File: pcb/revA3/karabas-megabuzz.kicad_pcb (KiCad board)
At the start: 4 copper layers, 92.2 x 44 mm, 173 parts, among them J1 FPGA JTAG, J2 Conn_02x31_Row_Letter_First, J3 uSD card, J4 PJ307, J5 Conn_01x04, J6 PRG, J7 NMI, T1 TestPoint1, T2 TestPoint2, T3 TestPoint, T4 TestPoint, T5 TestPoint, T6 TestPoint, T7 TestPoint, U1 XC6SLX25-FTG256, U10 YMF262-M, U11 SAM2695, U12 PCM5102A, U13 PCM1808PWR, U14 CY62167EV30LL, U15 1117-3.3, U16 1117-3.3, U17 1117-1.2, U18 APS6404L-3SQRx-SN, U19 74AHCT1G125DB, U2 W25Q128JVS, U20 AS6C1008-xxST, U21 24LC08, U22 VS1053, U23 XC6206P182MR, U3 74AHCT1G125DB, U4 74AHCT1G125DB, U5 SN74CB3T3245PW, U6 SN74CB3T3245PW, U7 SN74CB3T3245PW, U8 SN74CB3T3245PW, U9 SN74LV1T34DBV, X1 50 MHz

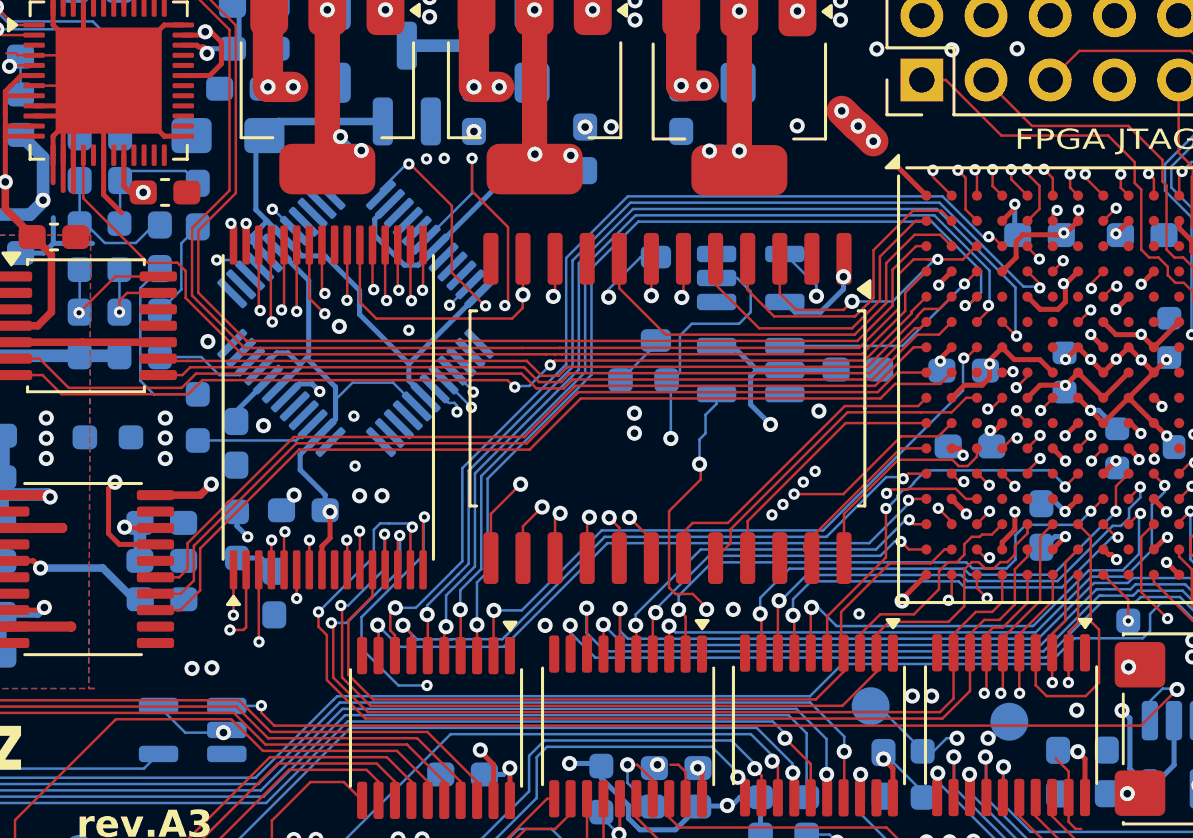
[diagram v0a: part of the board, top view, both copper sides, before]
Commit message: Neorv32 (#4)
* Added mp3dec sw for neorv32 risc-v cpu, added initial vhdl for neorv32

* working vs1053/vs1063 module

* Updated revA3 with required additional pullups

* vs1053 testbench

* neorv32 firmware update

* Added a test zx program to play test mp3

* playmp3 dot command for megabuzz

* outdated files

* Release bit files for A,A1,A2,A3 SLX16/25

* latest test build

* Updated comments

* Updated A3 errata

* Fixed buffer size

* browser plugin

* Reduced buffer size to 1024

* working plugin

* Optimized read/transfers

* Added keyboard navigation

* Updated plugin header, added ability to autoplay next file

* Updated revA3 with required pullups for vs10xx chip

* Updated readme
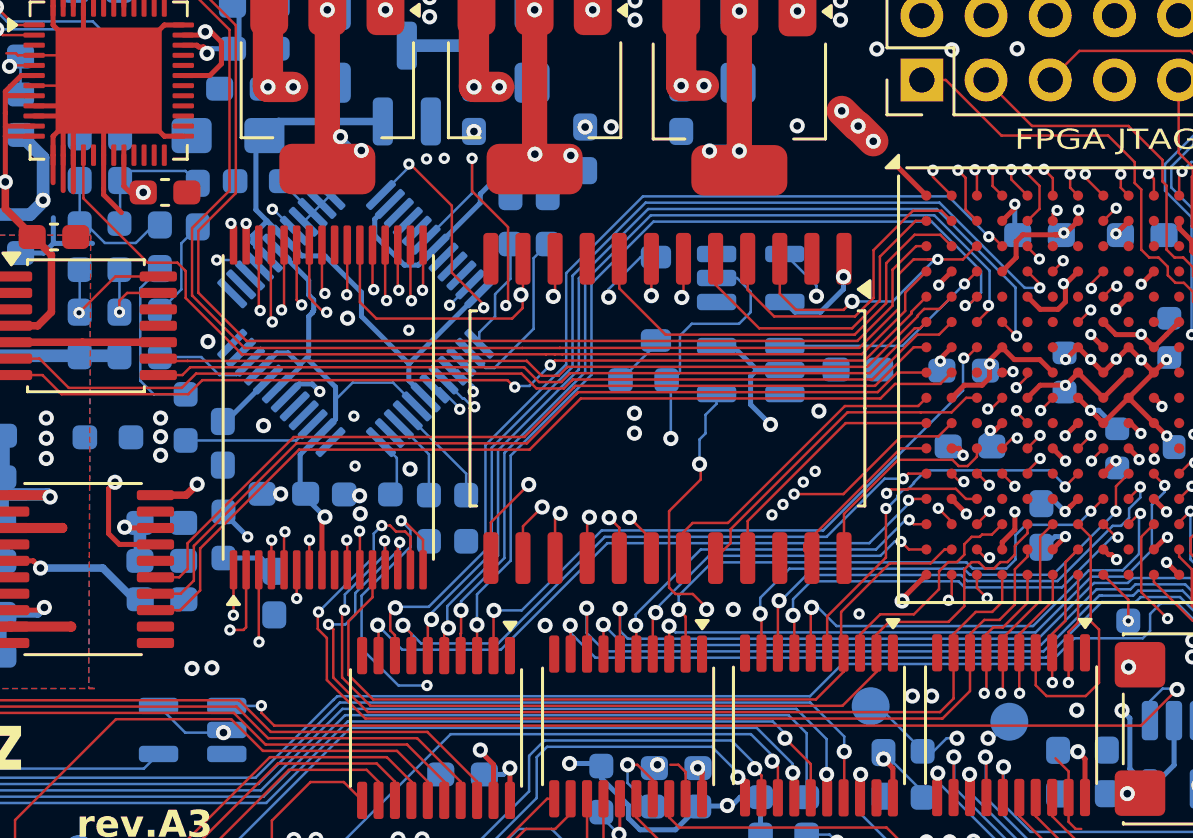
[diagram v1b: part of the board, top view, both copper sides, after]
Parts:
- added R16: 10k, Resistor_SMD:R_0603_1608Metric_Pad0.98x0.95mm_HandSolder, B.Cu at (142.5, 101.8)
- added R17: 100k, Resistor_SMD:R_0603_1608Metric_Pad0.98x0.95mm_HandSolder, B.Cu at (139.2, 113.6)
- added R18: 100k, Resistor_SMD:R_0603_1608Metric_Pad0.98x0.95mm_HandSolder, B.Cu at (137.8, 113.6)
- added R19: 100k, Resistor_SMD:R_0603_1608Metric_Pad0.98x0.95mm_HandSolder, B.Cu at (135.3, 112.6)
- added R29: 100k, Resistor_SMD:R_0603_1608Metric_Pad0.98x0.95mm_HandSolder, B.Cu at (141.0, 101.8)
- added R56: 100k, Resistor_SMD:R_0603_1608Metric_Pad0.98x0.95mm_HandSolder, B.Cu at (131.0, 100.2)
- moved C58 1.01 mm to (132.0, 112.6)
- moved C64 0.53 mm to (129.6, 110.6)
- moved R28 0.53 mm to (129.6, 114.2)
- moved R25 0.48 mm to (128.1, 109.6)
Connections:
- U22 pad 10: unconnected-(U22-GPIO3/SDATA-Pad10) -> Net-(U22-GPIO2/DCLK)
- U22 pad 11: unconnected-(U22-GPIO6/I2S_SCLK-Pad11) -> Net-(U22-GPIO2/DCLK)
- U22 pad 12: unconnected-(U22-GPIO7/I2S_SDATA-Pad12) -> Net-(U22-GPIO2/DCLK)
- U22 pad 25: unconnected-(U22-GPIO5/I2S_MCLK-Pad25) -> Net-(U22-GPIO5/I2S_MCLK)
- U22 pad 26: unconnected-(U22-RX-Pad26) -> Net-(U22-RX)
- U22 pad 33: unconnected-(U22-GPIO0-Pad33) -> Net-(U22-GPIO0)
- U22 pad 34: unconnected-(U22-GPIO1-Pad34) -> Net-(U22-GPIO1)
- U22 pad 36: unconnected-(U22-GPIO4/I2S_LROUT-Pad36) -> Net-(U22-GPIO4/I2S_LROUT)
- U22 pad 9: unconnected-(U22-GPIO2/DCLK-Pad9) -> Net-(U22-GPIO2/DCLK)
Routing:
- net Net-(U22-RX): track 0.00 -> 6.98 mm
- net Net-(U22-GPIO5/I2S_MCLK): track 0.00 -> 4.46 mm
- net Net-(U22-GPIO0): track 0.00 -> 4.12 mm
- net Net-(U22-GPIO1): track 0.00 -> 3.30 mm
- net Net-(U22-GPIO2/DCLK): track 0.00 -> 3.27 mm
- net Net-(U22-GPIO4/I2S_LROUT): track 0.00 -> 2.44 mm
- net +3V3: track 225.9 -> 227.6 mm
- net xA7: track 40.9 -> 40.2 mm
- net xD1: track 71.6 -> 72.2 mm
- net GND: vias 123 -> 124
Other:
- board text removed: "Special thanks to Caasper911"

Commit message: Updated revA3 - the reset output on bss138
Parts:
- removed D18: 1N4148W, Diode_SMD:D_SOD-123
- added Q1: BSS138, Package_TO_SOT_SMD:SOT-23, B.Cu at (145.9, 106.4)
- added R57: 10k, Resistor_SMD:R_0603_1608Metric_Pad0.98x0.95mm_HandSolder, B.Cu at (150.7, 110.8)
- R53: value 27 -> 10k
- moved R53 4.82 mm to (146.2, 103.3), turned to 180 degrees
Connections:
- R53 pad 1: Net-(D18-A) -> +3V3
- R53 pad 2: ~{RST} -> ~{oRST}
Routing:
- net +3V3: track 227.6 -> 240.0 mm
- net ~{RST}: track 38.1 -> 43.8 mm
- net Net-(D18-A): track 2.15 -> 0.00 mm
- net +5V: track 233.5 -> 234.6 mm
- net xD7: track 70.9 -> 71.9 mm
- net xD6: track 75.5 -> 76.6 mm
- net xD1: track 72.2 -> 73.2 mm
- net xA13: track 36.1 -> 37.1 mm
- net xD0: track 74.2 -> 75.2 mm
- net ~{xRD}: track 30.1 -> 29.5 mm
- net GND: track 126.2 -> 126.1 mm, vias 124 -> 123
